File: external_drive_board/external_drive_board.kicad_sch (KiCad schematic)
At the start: 26 parts, among them J1 MD-90SM, J2 MD-90SM, J3 Conn_02x17_Odd_Even, J4 Conn_01x04, J5 Conn_01x02, J6 Conn_01x02, J7 Conn_01x02, SW1 SW_DIP_x04, U1 74LS125, U2 74LS85, U3 74LS595, U4 74LS165, U5 74LS04

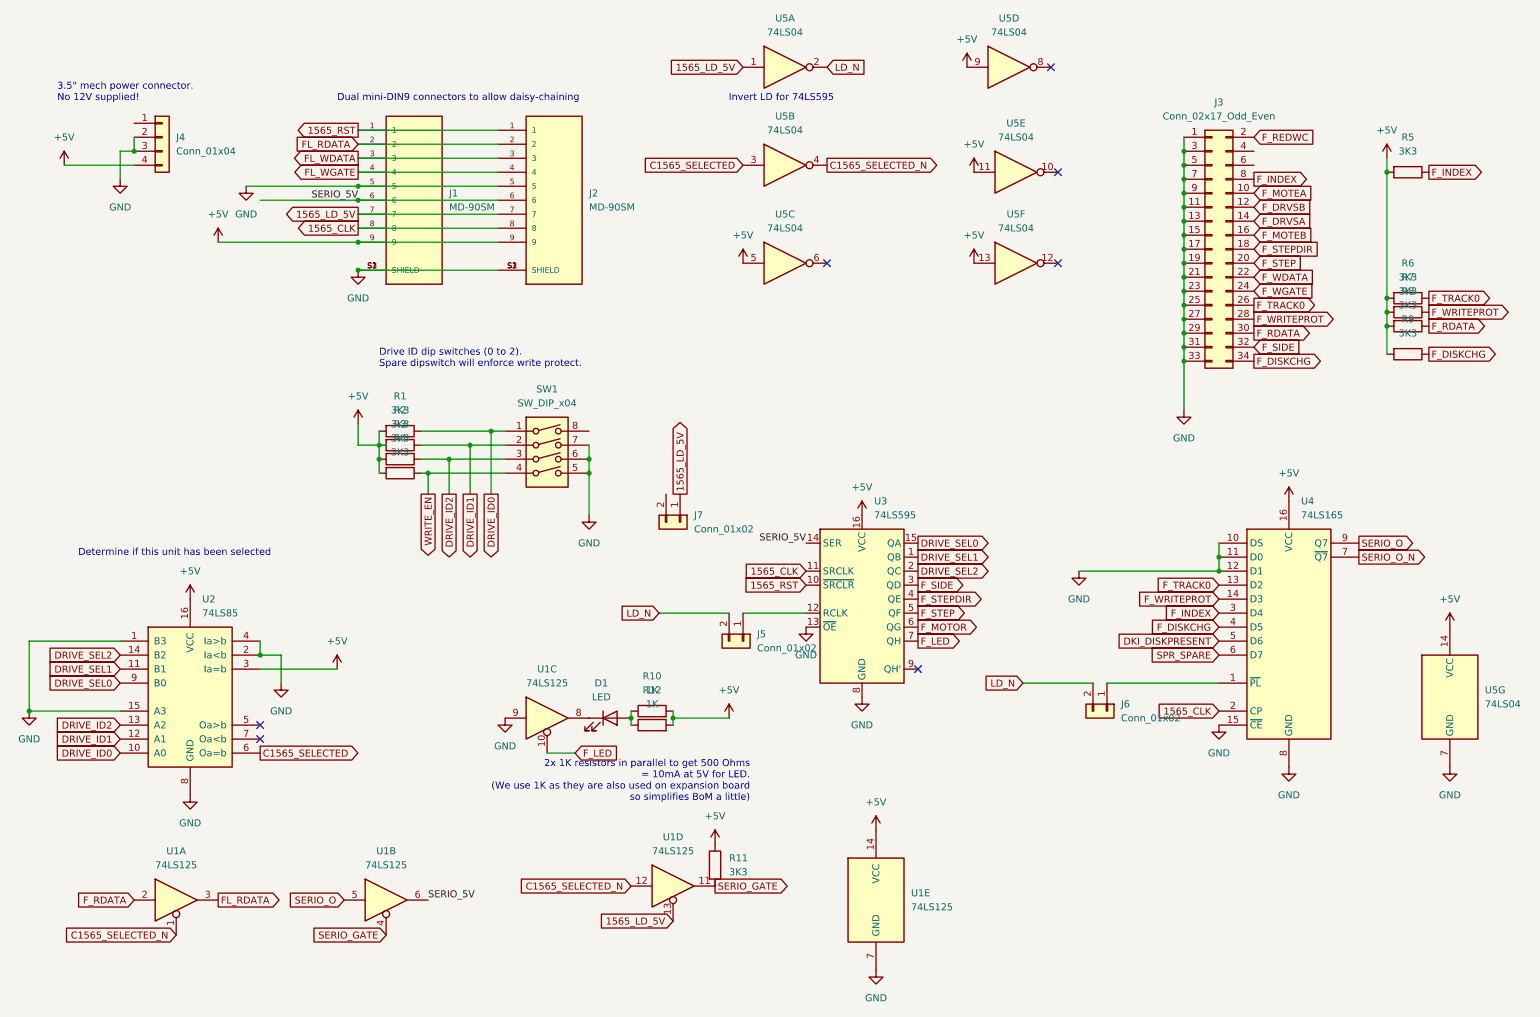
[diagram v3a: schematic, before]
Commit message: add dipsw reading to M1565 via spare bit
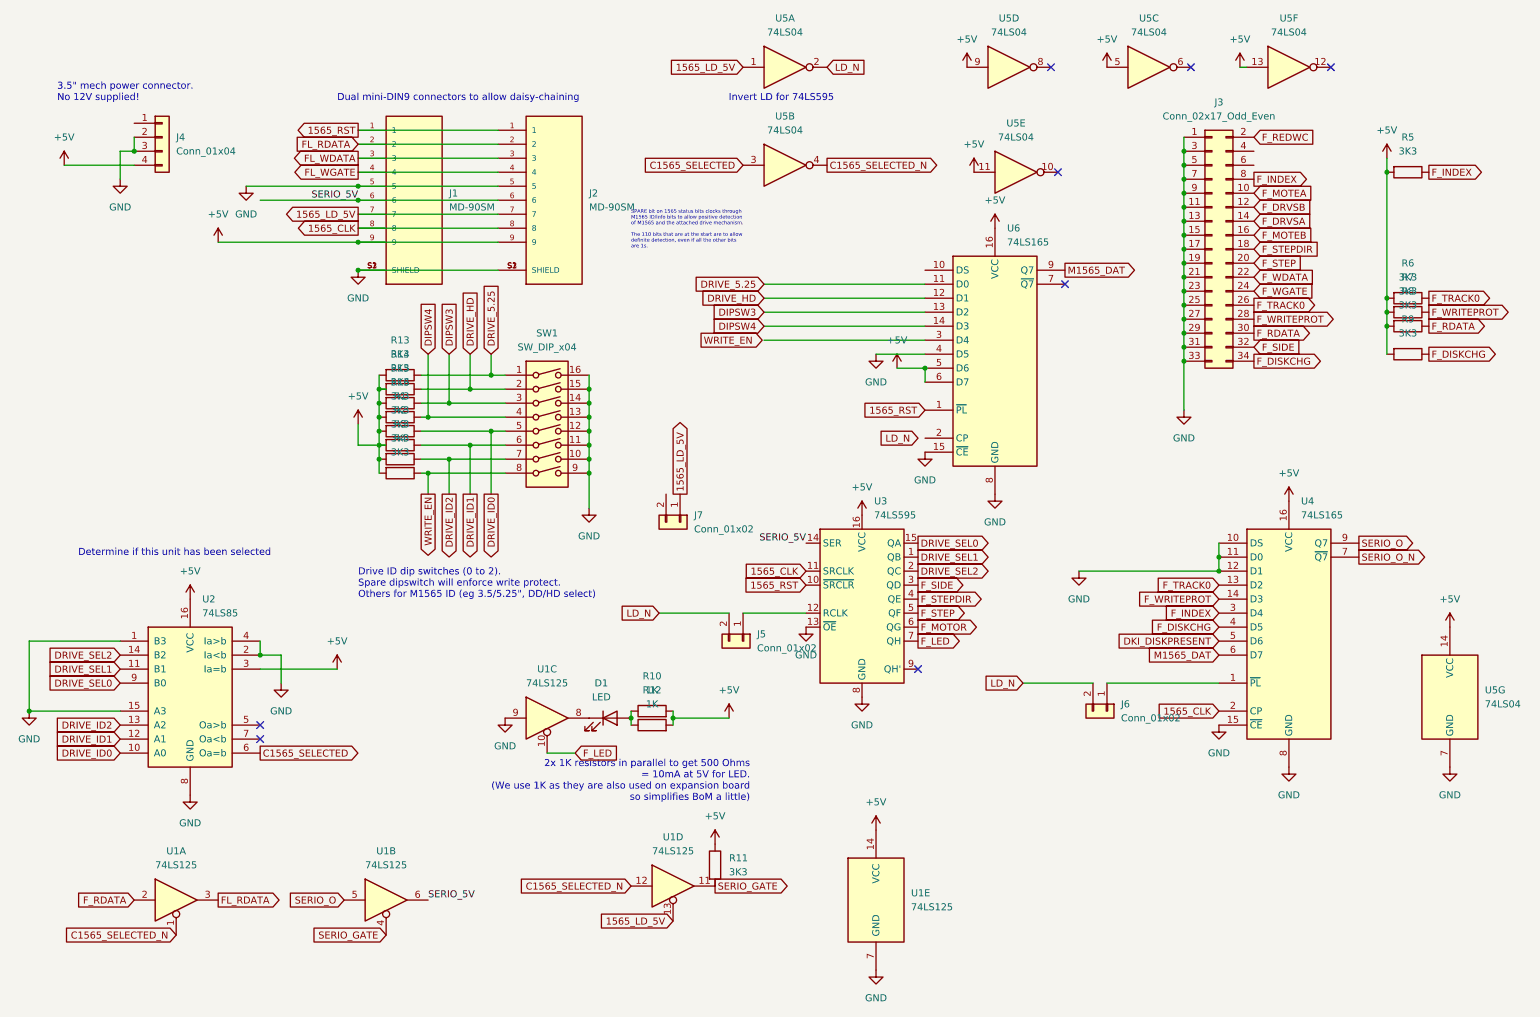
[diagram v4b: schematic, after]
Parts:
- added R13, R14, R15, R16: 3K3, Resistor_THT:R_Axial_DIN0207_L6.3mm_D2.5mm_P7.62mm_Horizontal, symbol Device:R
- added U6: 74LS165, Package_DIP:DIP-16_W7.62mm, symbol 74xx:74LS165
- SW1: footprint Package_DIP:DIP-8_W7.62mm -> Package_DIP:DIP-16_W7.62mm; symbol Switch:SW_DIP_x04 -> Switch:SW_DIP_x08
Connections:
- net +5V: now also R13.2, R14.2, R15.2, R16.2, U6.16 (VCC), U6.5 (D6), U6.6 (D7)
- net 1565_RST: now also U6.1 (~{PL})
- net DRIVE_ID0: now also SW1.5; no longer SW1.1
- net DRIVE_ID1: now also SW1.6; no longer SW1.2
- net DRIVE_ID2: now also SW1.7; no longer SW1.3
- net GND: now also SW1.10, SW1.11, SW1.12, SW1.13, SW1.14, SW1.15, SW1.16, SW1.9, U6.15 (~{CE}), U6.4 (D5), U6.8 (GND); no longer SW1.5, SW1.6, SW1.7
- net WRITE_EN: now also SW1.8; no longer SW1.4
- net SPR_SPARE renamed M1565_DAT
- net M1565_DAT: now also U6.9 (Q7)
- new net DIPSW3: R15.1, SW1.3, U6.13 (D2)
- new net DIPSW4: R16.1, SW1.4, U6.14 (D3)
- new net DRIVE_5.25: R13.1, SW1.1, U6.11 (D0)
- new net DRIVE_HD: R14.1, SW1.2, U6.12 (D1)
- no-connect marks 7 -> 8
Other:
- note added: "Drive ID dip switches (0 to 2). Spare dipswitch will enforce write protect. Others for M1565 ID (eg 3.5/5.25", DD/HD select)"
- note added: "SPARE bit on 1565 status bits clocks through M1565 ID/info bits to allow positive detection of M1565 and the attached drive mechanism. The 110 bits that are at the start are to allow definite detection, even if all the other bits are 1s."
- note removed: "Drive ID dip switches (0 to 2). Spare dipswitch will enforce write protect."
- moved on the sheet: U5C, U5F

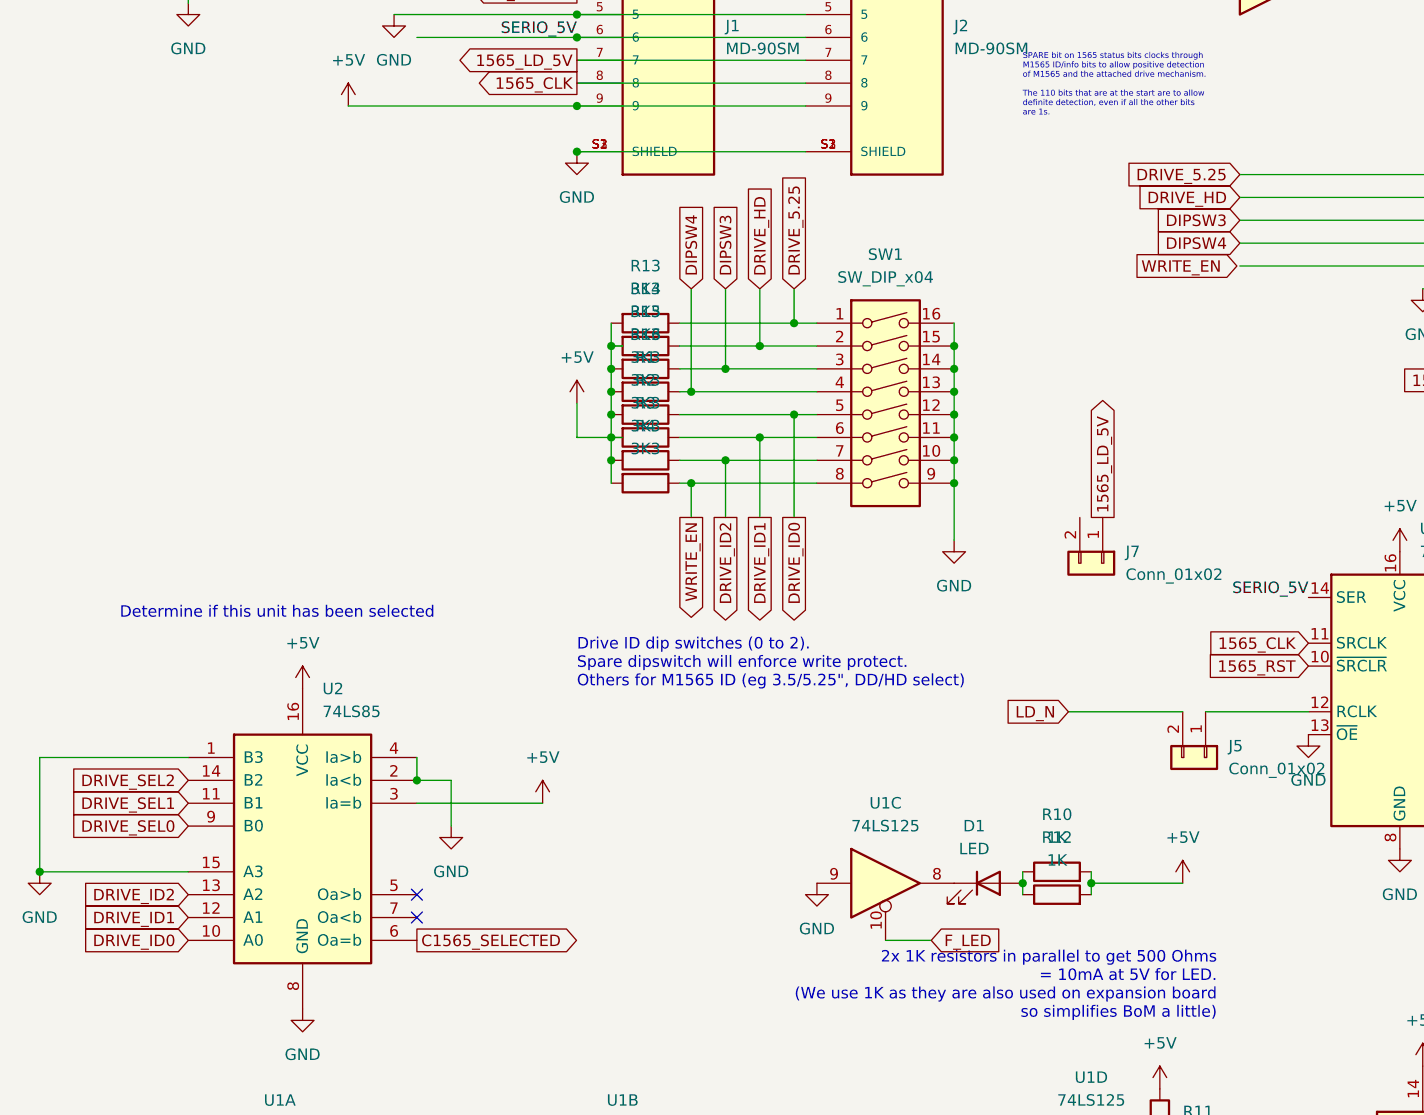
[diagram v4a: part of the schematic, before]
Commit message: route +5V and GND on M1565 board
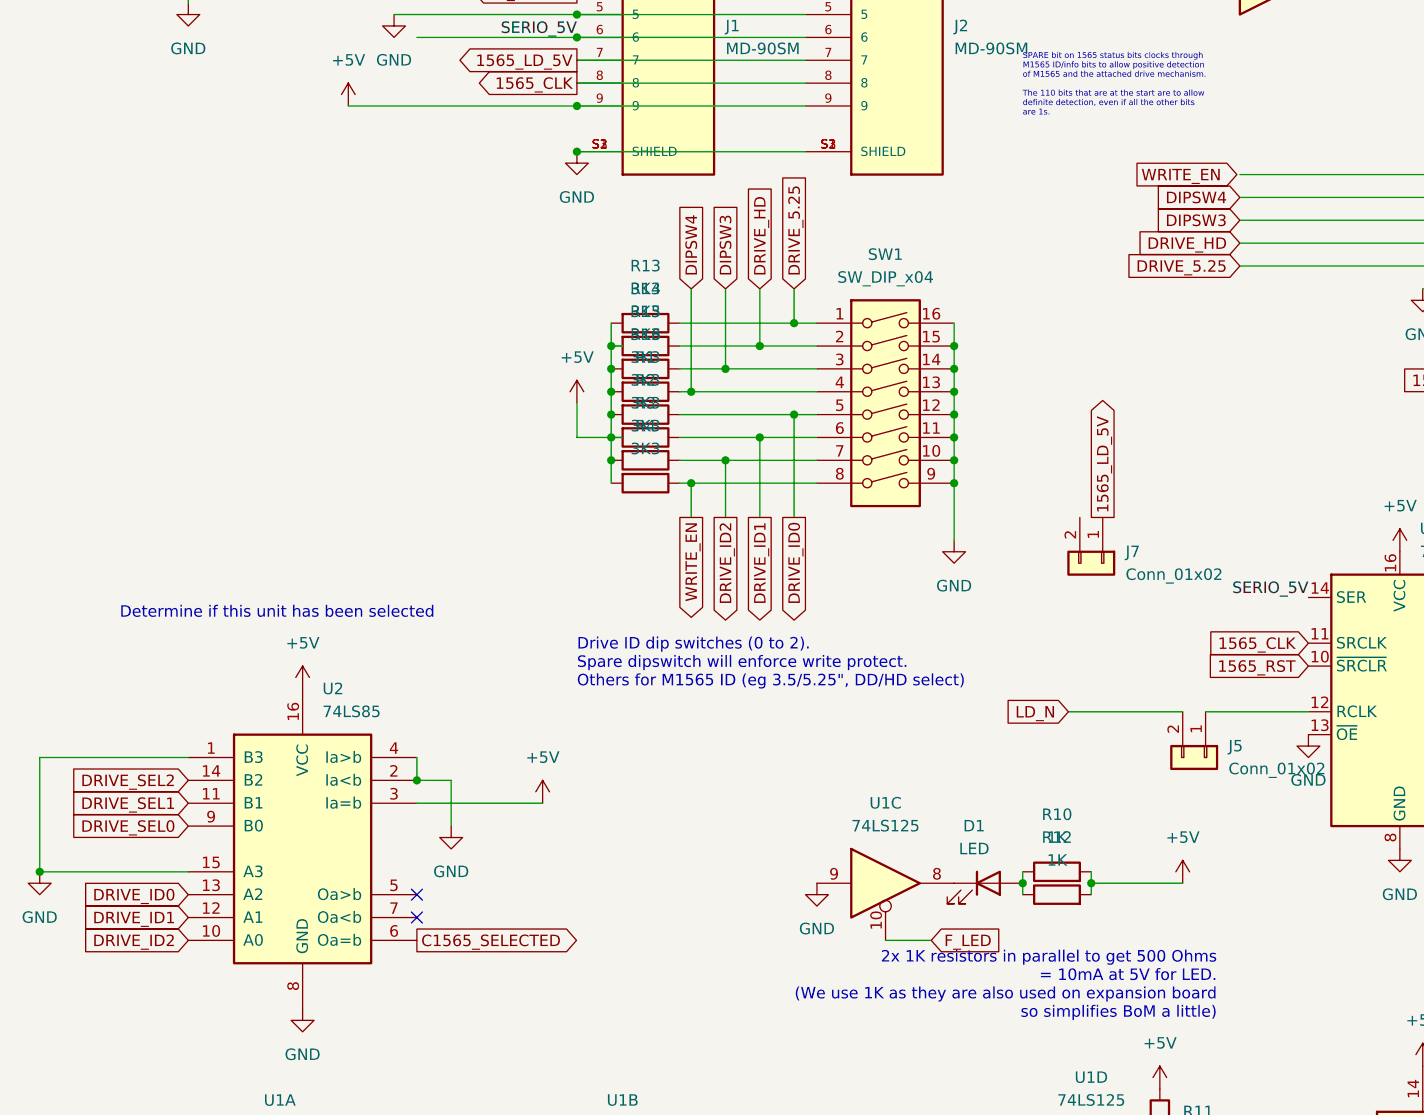
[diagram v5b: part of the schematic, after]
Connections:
- net DIPSW4: now also U6.12 (D1); no longer U6.14 (D3)
- net DRIVE_5.25: now also U6.3 (D4); no longer U6.11 (D0)
- net DRIVE_HD: now also U6.14 (D3); no longer U6.12 (D1)
- net DRIVE_ID0: now also U2.13 (A2); no longer U2.10 (A0)
- net DRIVE_ID2: now also U2.10 (A0); no longer U2.13 (A2)

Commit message: more routing
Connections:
- net FL_WDATA is gone; now on net F_WDATA: J1.3, J2.3
- net FL_WGATE is gone; now on net F_WGATE: J1.4, J2.4
- net FL_RDATA renamed F_RDATA_GATED
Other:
- moved on the sheet: U1A

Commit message: more work on M1565 board
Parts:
- removed J5, J6, J7: Conn_01x02, Connector_PinHeader_2.54mm:PinHeader_1x02_P2.54mm_Vertical, symbol Connector_Generic:Conn_01x02
- added H1, H2, H3: MountingHole, MountingHole:MountingHole_3mm_Pad, symbol Mechanical:MountingHole
- added J5, J7: Conn_01x03, Connector_PinHeader_2.54mm:PinHeader_1x03_P2.54mm_Vertical, symbol Connector_Generic:Conn_01x03
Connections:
- net F_DRVSA is gone; now on net C1565_SELECTED_N: J3.14 (Pin_14)
- net F_DRVSB is gone; now on net C1565_SELECTED_N: J3.12 (Pin_12)
- net F_MOTEB is gone; now on net F_MOTEA: J3.16 (Pin_16)
- net F_MOTOR is gone; now on net F_MOTEA: U3.6 (QG)
- net 1565_LD_5V: now also J5.3 (Pin_3), J7.3 (Pin_3)
- net LD_N: now also J5.1 (Pin_1), J7.1 (Pin_1)
- net at U4.1 (~{PL}): now also J7.2 (Pin_2)
- net at U3.12 (RCLK): now also J5.2 (Pin_2)

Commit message: finish M1565 initial board rev
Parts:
- added H4: MountingHole, MountingHole:MountingHole_3mm_Pad, symbol Mechanical:MountingHole
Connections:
- net DIPSW3 renamed DENSITY1
- net DRIVE_HD renamed DENSITY0
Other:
- note added: "Drive ID dip switches (0 to 2). Spare dipswitch will enforce write protect. Others for M1565 ID (eg 3.5/5.25", DD/HD select) NOTE: Write protect dip switch can be overriden by FPGA in the MEGA65 -- its only an advisory, because we ran out of 74LS125 gates to be able to actually gate the WGATE signal based on WRITE_EN"
- note removed: "Drive ID dip switches (0 to 2). Spare dipswitch will enforce write protect. Others for M1565 ID (eg 3.5/5.25", DD/HD select)"
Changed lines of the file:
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@@
     (effects (font (size 1.27 1.27)) (justify left bottom))
   )
-  (text "Drive ID dip switches (0 to 2).\nSpare dipswitch will enforce write protect.\nOthers for M1565 ID (eg 3.5/5.25\", DD/HD select)"
-    (at 73.66 123.19 0)
+  (text "Drive ID dip switches (0 to 2).\nSpare dipswitch will enforce write protect.\nOthers for M1565 ID (eg 3.5/5.25\", DD/HD select)\n\nNOTE: Write protect dip switch can be overriden\nby FPGA in the MEGA65 -- its only an advisory,\nbecause we ran out of 74LS125 gates to be able to\nactually gate the WGATE signal based on WRITE_EN"
+    (at 67.31 132.08 0)
     (effects (font (size 1.27 1.27)) (justify left bottom))
   )
@@
     )
   )
-  (global_label "DIPSW3" (shape input) (at 147.32 71.12 180) (fields_autoplaced)
-    (effects (font (size 1.27 1.27)) (justify right))
-    (property "Intersheetrefs" "${INTERSHEET_REFS}" (at 137.3196 71.12 0)
+  (global_label "DENSITY1" (shape input) (at 147.32 71.12 180) (fields_autoplaced)
+    (effects (font (size 1.27 1.27)) (justify right))
+    (property "Intersheetrefs" "${INTERSHEET_REFS}" (at 135.5053 71.12 0)
       (effects (font (size 1.27 1.27)) (justify right) hide)
     )
@@
     )
   )
-  (global_label "DRIVE_HD" (shape input) (at 93.98 78.74 90) (fields_autoplaced)
-    (effects (font (size 1.27 1.27)) (justify left))
-    (property "Intersheetrefs" "${INTERSHEET_REFS}" (at 93.98 66.8043 90)
+  (global_label "DENSITY0" (shape input) (at 93.98 78.74 90) (fields_autoplaced)
+    (effects (font (size 1.27 1.27)) (justify left))
+    (property "Intersheetrefs" "${INTERSHEET_REFS}" (at 93.98 66.9253 90)
       (effects (font (size 1.27 1.27)) (justify left) hide)
     )
@@
     )
   )
-  (global_label "DIPSW3" (shape input) (at 90.17 78.74 90) (fields_autoplaced)
-    (effects (font (size 1.27 1.27)) (justify left))
-    (property "Intersheetrefs" "${INTERSHEET_REFS}" (at 90.17 68.7396 90)
+  (global_label "DENSITY1" (shape input) (at 90.17 78.74 90) (fields_autoplaced)
+    (effects (font (size 1.27 1.27)) (justify left))
+    (property "Intersheetrefs" "${INTERSHEET_REFS}" (at 90.17 66.9253 90)
       (effects (font (size 1.27 1.27)) (justify left) hide)
     )
@@
     )
   )
-  (global_label "DRIVE_HD" (shape input) (at 147.32 73.66 180) (fields_autoplaced)
-    (effects (font (size 1.27 1.27)) (justify right))
-    (property "Intersheetrefs" "${INTERSHEET_REFS}" (at 135.3843 73.66 0)
+  (global_label "DENSITY0" (shape input) (at 147.32 73.66 180) (fields_autoplaced)
+    (effects (font (size 1.27 1.27)) (justify right))
+    (property "Intersheetrefs" "${INTERSHEET_REFS}" (at 135.5053 73.66 0)
       (effects (font (size 1.27 1.27)) (justify right) hide)
     )
@@
         )
       )
+    )
+  )
+  (symbol (lib_id "Mechanical:MountingHole") (at 44.45 95.25 0) (unit 1)
+    (in_bom yes) (on_board yes) (dnp no) (fields_autoplaced)
+    (property "Reference" "H4" (at 46.99 93.98 0)
+      (effects (font (size 1.27 1.27)) (justify left))
+    )
+    (property "Value" "MountingHole" (at 46.99 96.52 0)
+      (effects (font (size 1.27 1.27)) (justify left))
+    )
+    (property "Footprint" "MountingHole:MountingHole_3mm_Pad" (at 44.45 95.25 0)
+      (effects (font (size 1.27 1.27)) hide)
+    )
+    (property "Datasheet" "~" (at 44.45 95.25 0)
+      (effects (font (size 1.27 1.27)) hide)
+    )
+    (instances
+      (project "external_drive_board"
+        (path "/0105c347-4e24-4e51-91e8-df67c5985c25"
+          (reference "H4") (unit 1)
+        )
+      )
